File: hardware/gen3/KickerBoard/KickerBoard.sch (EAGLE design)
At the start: 86 parts, among them IC1 TL331, Q3 MOSFET-NCHANNELFQP30N06L, Q4 MOSFET-NCHANNELBSS123LT1G, Q6 MOSFET-PCHANNEL, U1 NC7WZ08K8X, U2 ATMEGA165PV-8AU

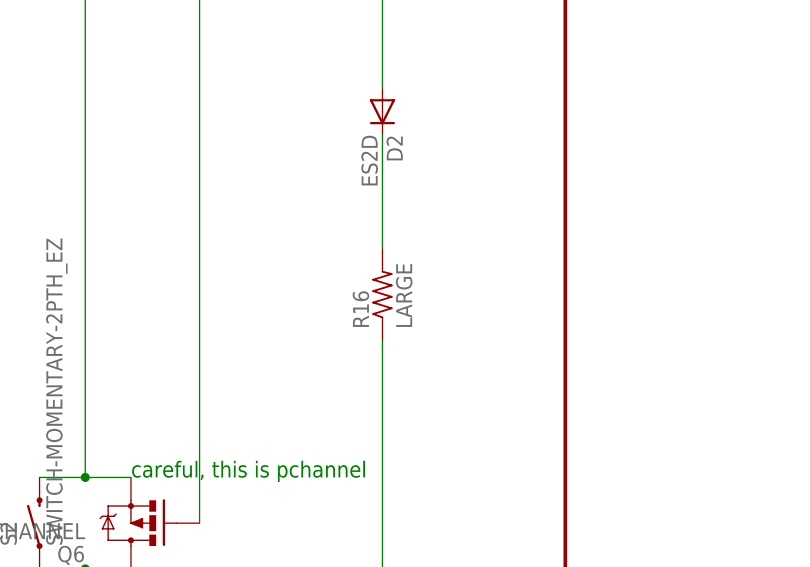
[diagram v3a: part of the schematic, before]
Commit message: discharge resistor value
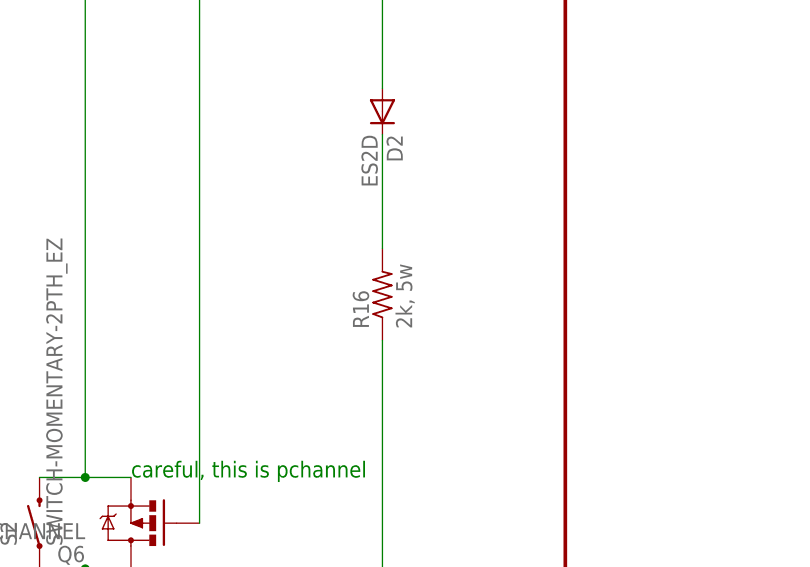
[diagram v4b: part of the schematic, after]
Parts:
- R16: value LARGE -> 2k, 5w
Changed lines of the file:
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@@
 <part name="KICK" library="SparkFun-Connectors" deviceset="M02" device="5MM"/>
 <part name="CHIP" library="SparkFun-Connectors" deviceset="M02" device="5MM"/>
-<part name="R16" library="rcl" deviceset="R-US_" device="R0805" value="LARGE"/>
+<part name="R16" library="rcl" deviceset="R-US_" device="R0805" value="2k, 5w"/>
 <part name="S2" library="SparkFun-Electromechanical" deviceset="SWITCH-MOMENTARY-2" device="PTH_EZ"/>
 <part name="FRAME2" library="SparkFun-Aesthetics" deviceset="FRAME-LETTER" device=""/>

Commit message: decoupling
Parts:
- added C13, C14, C15, C16: .1uF, SparkFun-Capacitors:CAP1206
- C10, C11: value >2.2uF -> 100uF
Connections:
- net 12V: now also C16.1
- net 12VGND: now also C16.2
- net 3.3V: now also C13.1
- net 5V: now also C14.1, C15.1
- net GND: now also C13.2, C14.2, C15.2
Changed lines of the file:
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@@
 <part name="TMP" library="SparkFun-Passives" deviceset="RESISTOR" device="0805-RES" value="0"/>
 <part name="S1" library="switch" deviceset="M9040P" device=""/>
-<part name="C10" library="SparkFun-Capacitors" deviceset="10UF-16V-10%(TANT)" device="" value="&gt;2.2uF"/>
-<part name="C11" library="SparkFun-Capacitors" deviceset="10UF-16V-10%(TANT)" device="" value="&gt;2.2uF"/>
+<part name="C10" library="SparkFun-Capacitors" deviceset="10UF-16V-10%(TANT)" device="" value="100uF"/>
+<part name="C11" library="SparkFun-Capacitors" deviceset="10UF-16V-10%(TANT)" device="" value="100uF"/>
 <part name="R13" library="SparkFun-Passives" deviceset="RESISTOR" device="1206" value="130"/>
 <part name="R17" library="SparkFun-Passives" deviceset="RESISTOR" device="1206" value="130"/>
@@
 <part name="LED8" library="SparkFun-LED" deviceset="LED" device="1206"/>
 <part name="Q3" library="SparkFun-DiscreteSemi" deviceset="MOSFET-NCHANNEL" device="FQP30N06L"/>
+<part name="C13" library="SparkFun-Capacitors" deviceset="CAP" device="1206" value=".1uF"/>
+<part name="C14" library="SparkFun-Capacitors" deviceset="CAP" device="1206" value=".1uF"/>
+<part name="C15" library="SparkFun-Capacitors" deviceset="CAP" device="1206" value=".1uF"/>
+<part name="C16" library="SparkFun-Capacitors" deviceset="CAP" device="1206" value=".1uF"/>
 </parts>
 <sheets>
@@
 <instance part="LED8" gate="G$1" x="73.66" y="238.76"/>
 <instance part="Q3" gate="G$1" x="487.68" y="76.2"/>
+<instance part="C13" gate="G$1" x="99.06" y="350.52"/>
+<instance part="C14" gate="G$1" x="99.06" y="320.04"/>
+<instance part="C15" gate="G$1" x="312.42" y="347.98"/>
+<instance part="C16" gate="G$1" x="434.34" y="342.9" rot="R90"/>
 </instances>
 <busses>
@@
 <pinref part="C10" gate="G$1" pin="-"/>
 <wire x1="86.36" y1="347.98" x2="86.36" y2="345.44" width="0.1524" layer="91"/>
-<label x="86.36" y="345.44" size="1.778" layer="95"/>
+<label x="91.44" y="345.44" size="1.778" layer="95"/>
+<pinref part="C13" gate="G$1" pin="2"/>
+<wire x1="99.06" y1="347.98" x2="99.06" y2="345.44" width="0.1524" layer="91"/>
+<wire x1="99.06" y1="345.44" x2="86.36" y2="345.44" width="0.1524" layer="91"/>
 </segment>
 <segment>
 <pinref part="C11" gate="G$1" pin="-"/>
 <wire x1="86.36" y1="317.5" x2="86.36" y2="314.96" width="0.1524" layer="91"/>
-<label x="86.36" y="314.96" size="1.778" layer="95"/>
+<label x="88.9" y="314.96" size="1.778" layer="95"/>
+<pinref part="C14" gate="G$1" pin="2"/>
+<wire x1="99.06" y1="317.5" x2="99.06" y2="314.96" width="0.1524" layer="91"/>
+<wire x1="99.06" y1="314.96" x2="86.36" y2="314.96" width="0.1524" layer="91"/>
 </segment>
 <segment>
@@
 <label x="53.34" y="226.06" size="1.778" layer="95"/>
 </segment>
+<segment>
+<pinref part="C15" gate="G$1" pin="2"/>
+<wire x1="312.42" y1="345.44" x2="312.42" y2="340.36" width="0.1524" layer="91"/>
+<label x="312.42" y="340.36" size="1.778" layer="95"/>
+</segment>
 </net>
 <net name="3.3V" class="0">
@@
 <wire x1="73.66" y1="358.14" x2="86.36" y2="358.14" width="0.1524" layer="91"/>
 <pinref part="C10" gate="G$1" pin="+"/>
-<wire x1="86.36" y1="358.14" x2="96.52" y2="358.14" width="0.1524" layer="91"/>
+<wire x1="86.36" y1="358.14" x2="99.06" y2="358.14" width="0.1524" layer="91"/>
+<wire x1="99.06" y1="358.14" x2="106.68" y2="358.14" width="0.1524" layer="91"/>
 <wire x1="86.36" y1="355.6" x2="86.36" y2="358.14" width="0.1524" layer="91"/>
 <junction x="86.36" y="358.14"/>
-<label x="96.52" y="358.14" size="1.778" layer="95"/>
+<label x="106.68" y="358.14" size="1.778" layer="95"/>
+<pinref part="C13" gate="G$1" pin="1"/>
+<wire x1="99.06" y1="355.6" x2="99.06" y2="358.14" width="0.1524" layer="91"/>
+<junction x="99.06" y="358.14"/>
 </segment>
 <segment>
@@
 <wire x1="429.26" y1="284.48" x2="429.26" y2="302.26" width="0.1524" layer="91"/>
 <pinref part="OK1" gate="A" pin="COL"/>
-<wire x1="429.26" y1="302.26" x2="429.26" y2="355.6" width="0.1524" layer="91"/>
+<wire x1="429.26" y1="302.26" x2="429.26" y2="342.9" width="0.1524" layer="91"/>
+<wire x1="429.26" y1="342.9" x2="429.26" y2="355.6" width="0.1524" layer="91"/>
 <wire x1="424.18" y1="302.26" x2="429.26" y2="302.26" width="0.1524" layer="91"/>
 <junction x="429.26" y="302.26"/>
 <label x="429.26" y="355.6" size="1.778" layer="95"/>
+<pinref part="C16" gate="G$1" pin="1"/>
+<junction x="429.26" y="342.9"/>
 </segment>
 <segment>
@@
 <label x="459.74" y="45.72" size="1.778" layer="95"/>
 </segment>
+<segment>
+<pinref part="C16" gate="G$1" pin="2"/>
+<wire x1="436.88" y1="342.9" x2="436.88" y2="337.82" width="0.1524" layer="91"/>
+<label x="431.8" y="337.82" size="1.778" layer="95"/>
+</segment>
 </net>
 <net name="N$5" class="0">
@@
 <segment>
 <pinref part="5REG" gate="G$1" pin="OUT"/>
-<label x="96.52" y="327.66" size="1.778" layer="95"/>
+<label x="106.68" y="327.66" size="1.778" layer="95"/>
 <wire x1="73.66" y1="327.66" x2="86.36" y2="327.66" width="0.1524" layer="91"/>
 <pinref part="C11" gate="G$1" pin="+"/>
-<wire x1="86.36" y1="327.66" x2="96.52" y2="327.66" width="0.1524" layer="91"/>
+<wire x1="86.36" y1="327.66" x2="99.06" y2="327.66" width="0.1524" layer="91"/>
+<wire x1="99.06" y1="327.66" x2="106.68" y2="327.66" width="0.1524" layer="91"/>
 <wire x1="86.36" y1="325.12" x2="86.36" y2="327.66" width="0.1524" layer="91"/>
 <junction x="86.36" y="327.66"/>
+<pinref part="C14" gate="G$1" pin="1"/>
+<wire x1="99.06" y1="325.12" x2="99.06" y2="327.66" width="0.1524" layer="91"/>
+<junction x="99.06" y="327.66"/>
 </segment>
 <segment>
@@
 <wire x1="340.36" y1="309.88" x2="330.2" y2="309.88" width="0.1524" layer="91"/>
 <junction x="330.2" y="309.88"/>
-</segment>
-</net>
+<pinref part="C15" gate="G$1" pin="1"/>
+<junction x="312.42" y="353.06"/>
+</segment>
+</net>

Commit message: fixed current limiting
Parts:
- C12, C4: value 100nF -> .1uF
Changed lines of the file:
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@@
 <part name="R29" library="SparkFun-Passives" deviceset="RESISTOR" device="1206" value="10k"/>
 <part name="Q6" library="SparkFun-DiscreteSemi" deviceset="MOSFET-PCHANNEL" device=""/>
-<part name="C4" library="SparkFun-Capacitors" deviceset="CAP" device="0805" value="100nF"/>
-<part name="C12" library="SparkFun-Capacitors" deviceset="CAP" device="0805" value="100nF"/>
+<part name="C4" library="SparkFun-Capacitors" deviceset="CAP" device="0805" value=".1uF"/>
+<part name="C12" library="SparkFun-Capacitors" deviceset="CAP" device="0805" value=".1uF"/>
 <part name="R30" library="SparkFun-Passives" deviceset="RESISTOR" device="0805-RES" value="10k"/>
 <part name="U2" library="Atmel_By_element14_Batch_1-00" deviceset="ATMEGA165PV-8AU" device=""/>

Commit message: Added programmer port to boards
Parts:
- removed PROG_CNT: (no value), SparkFun-Connectors:M03X22X3_SILK_MALE_PTH
- added JP1: M05X2PTH, SparkFun-Connectors:M05X2PTH
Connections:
- net 3.3V: now also JP1.2; no longer PROG_CNT.2
- net GND: now also JP1.10, JP1.4, JP1.6, JP1.8; no longer PROG_CNT.6
- net MISO: now also JP1.9; no longer PROG_CNT.1
- net MOSI: now also JP1.1; no longer PROG_CNT.4
- net RESET: now also JP1.5; no longer PROG_CNT.5
- net SCK: now also JP1.7; no longer PROG_CNT.3
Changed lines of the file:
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@@
 <part name="R3" library="SparkFun-Passives" deviceset="RESISTOR" device="0805-RES" value="10k"/>
 <part name="R4" library="SparkFun-Passives" deviceset="RESISTOR" device="0805-RES" value="10k"/>
-<part name="PROG_CNT" library="SparkFun-Connectors" deviceset="M03X2" device="2X3_SILK_MALE_PTH"/>
 <part name="U$3" library="kickerchips" deviceset="32052-TRANSFORMER" device=""/>
 <part name="Q5" library="rfc" deviceset="N-MOSFET" device=""/>
@@
 <part name="C15" library="SparkFun-Capacitors" deviceset="CAP" device="1206" value=".1uF"/>
 <part name="C16" library="SparkFun-Capacitors" deviceset="CAP" device="1206" value=".1uF"/>
+<part name="JP1" library="SparkFun-Connectors" deviceset="M05X2" device="PTH"/>
 </parts>
 <sheets>
@@
 <instance part="R3" gate="G$1" x="208.28" y="170.18"/>
 <instance part="R4" gate="G$1" x="203.2" y="167.64"/>
-<instance part="PROG_CNT" gate="G$1" x="93.98" y="27.94"/>
 <instance part="U$3" gate="G$1" x="421.64" y="124.46"/>
 <instance part="Q5" gate="G$1" x="381" y="101.6"/>
@@
 <instance part="C15" gate="G$1" x="312.42" y="347.98"/>
 <instance part="C16" gate="G$1" x="434.34" y="342.9" rot="R90"/>
+<instance part="JP1" gate="G$1" x="71.12" y="38.1"/>
 </instances>
 <busses>
@@
 <nets>
 <net name="GND" class="0">
-<segment>
-<pinref part="PROG_CNT" gate="G$1" pin="6"/>
-<wire x1="101.6" y1="25.4" x2="106.68" y2="25.4" width="0.1524" layer="91"/>
-<label x="101.6" y="25.4" size="1.778" layer="95"/>
-</segment>
 <segment>
 <wire x1="27.94" y1="149.86" x2="30.48" y2="149.86" width="0.1524" layer="91"/>
@@
 <label x="312.42" y="340.36" size="1.778" layer="95"/>
 </segment>
+<segment>
+<pinref part="JP1" gate="G$1" pin="10"/>
+<wire x1="78.74" y1="33.02" x2="81.28" y2="33.02" width="0.1524" layer="91"/>
+<pinref part="JP1" gate="G$1" pin="8"/>
+<wire x1="81.28" y1="33.02" x2="83.82" y2="33.02" width="0.1524" layer="91"/>
+<wire x1="78.74" y1="35.56" x2="81.28" y2="35.56" width="0.1524" layer="91"/>
+<wire x1="81.28" y1="35.56" x2="81.28" y2="33.02" width="0.1524" layer="91"/>
+<junction x="81.28" y="33.02"/>
+<pinref part="JP1" gate="G$1" pin="6"/>
+<wire x1="78.74" y1="38.1" x2="81.28" y2="38.1" width="0.1524" layer="91"/>
+<wire x1="81.28" y1="38.1" x2="81.28" y2="35.56" width="0.1524" layer="91"/>
+<junction x="81.28" y="35.56"/>
+<pinref part="JP1" gate="G$1" pin="4"/>
+<wire x1="78.74" y1="40.64" x2="81.28" y2="40.64" width="0.1524" layer="91"/>
+<wire x1="81.28" y1="40.64" x2="81.28" y2="38.1" width="0.1524" layer="91"/>
+<junction x="81.28" y="38.1"/>
+<label x="83.82" y="33.02" size="1.778" layer="95"/>
+</segment>
 </net>
 <net name="3.3V" class="0">
-<segment>
-<pinref part="PROG_CNT" gate="G$1" pin="2"/>
-<wire x1="101.6" y1="30.48" x2="106.68" y2="30.48" width="0.1524" layer="91"/>
-<label x="101.6" y="30.48" size="1.778" layer="95"/>
-</segment>
 <segment>
 <pinref part="LOGIC_HEADER" gate="G$1" pin="3"/>
@@
 <label x="93.98" y="154.94" size="1.778" layer="95"/>
 </segment>
+<segment>
+<pinref part="JP1" gate="G$1" pin="2"/>
+<wire x1="78.74" y1="43.18" x2="83.82" y2="43.18" width="0.1524" layer="91"/>
+<label x="81.28" y="43.18" size="1.778" layer="95"/>
+</segment>
 </net>
 <net name="MOSI" class="0">
@@
 </segment>
 <segment>
-<pinref part="PROG_CNT" gate="G$1" pin="4"/>
-<wire x1="101.6" y1="27.94" x2="106.68" y2="27.94" width="0.1524" layer="91"/>
-<label x="101.6" y="27.94" size="1.778" layer="95"/>
-</segment>
-<segment>
 <pinref part="U2" gate="A" pin="PB2"/>
 <wire x1="101.6" y1="111.76" x2="93.98" y2="111.76" width="0.1524" layer="91"/>
 <label x="93.98" y="111.76" size="1.778" layer="95"/>
 </segment>
+<segment>
+<pinref part="JP1" gate="G$1" pin="1"/>
+<wire x1="63.5" y1="43.18" x2="58.42" y2="43.18" width="0.1524" layer="91"/>
+<label x="55.88" y="43.18" size="1.778" layer="95"/>
+</segment>
 </net>
 <net name="MISO" class="0">
@@
 </segment>
 <segment>
-<pinref part="PROG_CNT" gate="G$1" pin="1"/>
-<wire x1="86.36" y1="30.48" x2="81.28" y2="30.48" width="0.1524" layer="91"/>
-<label x="81.28" y="30.48" size="1.778" layer="95"/>
-</segment>
-<segment>
 <pinref part="U2" gate="A" pin="PB3"/>
 <wire x1="101.6" y1="109.22" x2="93.98" y2="109.22" width="0.1524" layer="91"/>
 <label x="93.98" y="109.22" size="1.778" layer="95"/>
 </segment>
+<segment>
+<pinref part="JP1" gate="G$1" pin="9"/>
+<wire x1="63.5" y1="33.02" x2="58.42" y2="33.02" width="0.1524" layer="91"/>
+<label x="55.88" y="33.02" size="1.778" layer="95"/>
+</segment>
 </net>
 <net name="SCK" class="0">
@@
 </segment>
 <segment>
-<pinref part="PROG_CNT" gate="G$1" pin="3"/>
-<wire x1="86.36" y1="27.94" x2="81.28" y2="27.94" width="0.1524" layer="91"/>
-<label x="81.28" y="27.94" size="1.778" layer="95"/>
+<pinref part="JP1" gate="G$1" pin="7"/>
+<wire x1="63.5" y1="35.56" x2="58.42" y2="35.56" width="0.1524" layer="91"/>
+<label x="55.88" y="35.56" size="1.778" layer="95"/>
 </segment>
 </net>
@@
 <net name="RESET" class="0">
 <segment>
-<wire x1="88.9" y1="25.4" x2="86.36" y2="25.4" width="0.1524" layer="91"/>
-<label x="78.74" y="25.4" size="1.778" layer="95"/>
-<pinref part="PROG_CNT" gate="G$1" pin="5"/>
-<wire x1="86.36" y1="25.4" x2="81.28" y2="25.4" width="0.1524" layer="91"/>
-<junction x="86.36" y="25.4"/>
-</segment>
-<segment>
 <pinref part="U2" gate="A" pin="~RESET/PG5"/>
 <wire x1="147.32" y1="139.7" x2="154.94" y2="139.7" width="0.1524" layer="91"/>
 <label x="149.86" y="139.7" size="1.778" layer="95"/>
 </segment>
-</net>
+<segment>
+<pinref part="JP1" gate="G$1" pin="5"/>
+<wire x1="63.5" y1="38.1" x2="58.42" y2="38.1" width="0.1524" layer="91"/>
+<label x="55.88" y="38.1" size="1.778" layer="95"/>
+</segment>
+</net>

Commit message: parts
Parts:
- removed S1: (no value), switch:M9040P
- removed S2: SWITCH-MOMENTARY-2PTH_EZ, SparkFun-Electromechanical:SWITCH-MOMENTARY-2PTH_EZ
- added MAN-DIS: SWITCH-MOMENTARY-2SMD-4, SparkFun-Electromechanical:SWITCH-MOMENTARY-2SMD-4
- added ON/OFF: SPDT-SWITCH, gen3:SPDT-SWITCH
- U$1, U$2: value TVS -> TVSSMA; device SparkFun-DiscreteSemi:TVS -> SparkFun-DiscreteSemi:TVSSMA
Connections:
- net 12V: now also ON/OFF.P2; no longer S1.S
- net 12V.: now also MAN-DIS.2; no longer S2.2
- net CAP+: now also U$1.C, U$2.C; no longer U$1.2, U$2.2
- net N$19: now also ON/OFF.COM; no longer S1.P
- net N$33: now also U$2.A; no longer U$2.1
- net N$34: now also U$1.A; no longer U$1.1
- net N$41: now also MAN-DIS.1; no longer S2.1
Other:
- moved on the sheet: BATT-1
